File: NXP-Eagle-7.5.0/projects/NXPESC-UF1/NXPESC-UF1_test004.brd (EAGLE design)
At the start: 59.7 x 20.6 mm, 75 parts, among them P1 MOT_PWR_PAD-1, P2 MOT_PWR_PAD-1, P3 MOT_PWR_PAD-1, P4 MOT_PWR_PAD-1, P5 MOT_PWR_PAD-1, U1 DF13-4P-1.25H, U10 PSMN1R4-30YLD, U11 PSMN1R4-30YLD, U12 PSMN1R4-30YLD, U13 PSMN1R4-30YLD, U15 TJA1042TK/3, U17 DF13-4P-1.25H, U2 MKV31F512VLH12-M, U8 PSMN1R4-30YLD, U9 PSMN1R4-30YLD

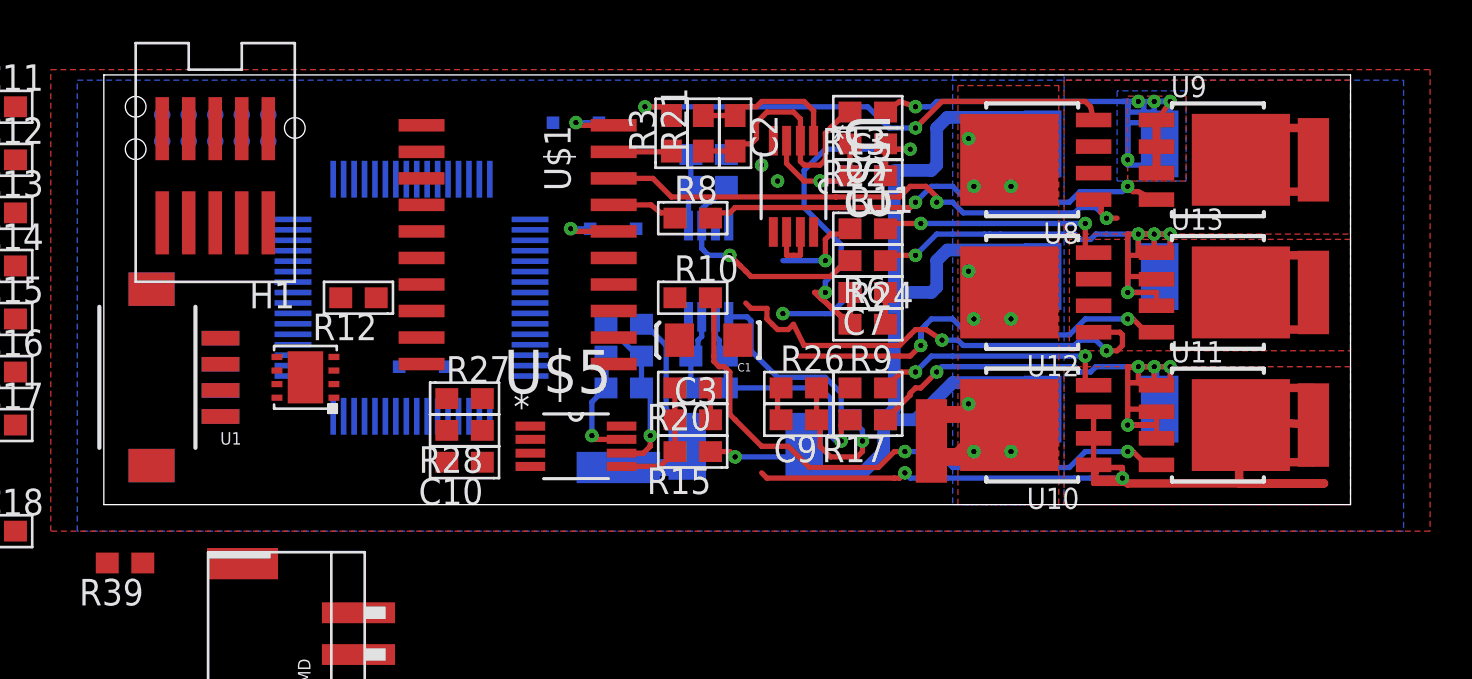
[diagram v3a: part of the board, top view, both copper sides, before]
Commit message: Majority of Power FET stage/gate driver and sense amplifiers are layed out. Moving on to finishing the MCU details.
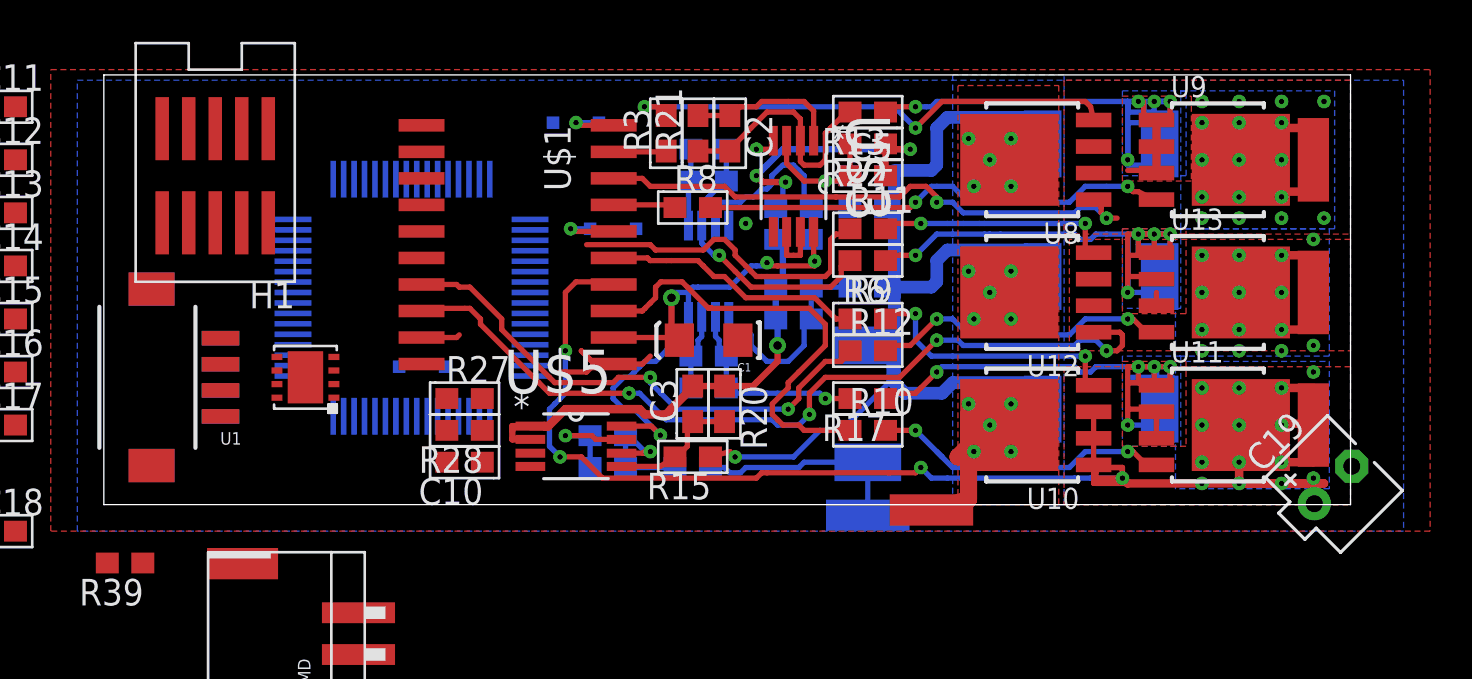
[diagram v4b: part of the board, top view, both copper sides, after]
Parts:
- removed H3: TC2050-IDCNH, etc-connector-003a:TC2050-IDC-NOHOLES
- added C19: (no value), etc-rcl:ETR1
- moved R12 24.5 mm to (36.6, 7.37), turned to 0 degrees
- moved P4 12.2 mm to (36.6, -0.51), turned to 180 degrees
- moved R10 10.5 mm to (36.6, 3.56)
- moved R16 7.61 mm to (28.2, 1.78)
- moved R18 6.35 mm to (36.6, 10.4)
- moved R5 6.19 mm to (36.6, 4.83), turned to 90 degrees
- moved C7 5.40 mm to (33.0, 14.2), flipped to the bottom, turned to 0 degrees
- moved R24 5.40 mm to (33.0, 12.7), flipped to the bottom, turned to 180 degrees
- moved C4 5.39 mm to (24.1, 1.78)
- moved C9 4.83 mm to (33.0, 8.89), flipped to the bottom, turned to 0 degrees
- moved R26 4.83 mm to (33.0, 10.4), flipped to the bottom, turned to 180 degrees
- moved R7 4.06 mm to (36.6, 14.2)
- moved R9 3.30 mm to (36.6, 8.89)
- moved P5 3.30 mm to (39.6, -0.25), turned to 0 degrees
- moved R19 2.41 mm to (24.1, 3.30)
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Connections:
- net +3V3: no longer H3.1
- net +V_MOTOR: now also C19.+
- net AGND: now also C19.-
- net GND: no longer H3.2, H3.3
- net RESET_B: no longer H3.6
- net SWD_CLK: no longer H3.9
- net SWD_DIO: no longer H3.10
- net TRACE_SWO: no longer H3.8
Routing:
- net +3V3: track 0.00 -> 27.4 mm, vias 0 -> 4
- net LOC: track 0.00 -> 25.1 mm, vias 0 -> 2
- net LOB: track 0.00 -> 21.9 mm
- net PH_B: track 61.5 -> 82.7 mm, vias 2 -> 18
- net PH_C: track 38.0 -> 56.4 mm, vias 2 -> 18
- net N$9: track 28.9 -> 14.6 mm
- net HOC: track 4.59 -> 17.7 mm, vias 1 -> 0
- net HOB: track 0.00 -> 12.5 mm
- net ADC_MID: track 30.6 -> 39.8 mm, vias 2 -> 4
- net GND: track 0.00 -> 7.87 mm
- net CS_C_L: track 5.28 -> 11.7 mm, vias 1 -> 0
- net N$17: track 20.7 -> 14.5 mm
- net CS_ABC_L/DCB_H: track 61.7 -> 56.0 mm
- net N$11: track 39.5 -> 45.0 mm
- net +V_MOTOR: track 8.55 -> 13.6 mm, vias 9 -> 15
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- added copper zone on layer 1, net N$11
- added copper zone on layer 16, net N$11
- added copper zone on layer 1, net N$12
- added copper zone on layer 16, net N$12
- added copper zone on layer 16, net PH_A
- added copper zone on layer 16, net PH_B
- added copper zone on layer 16, net PH_C

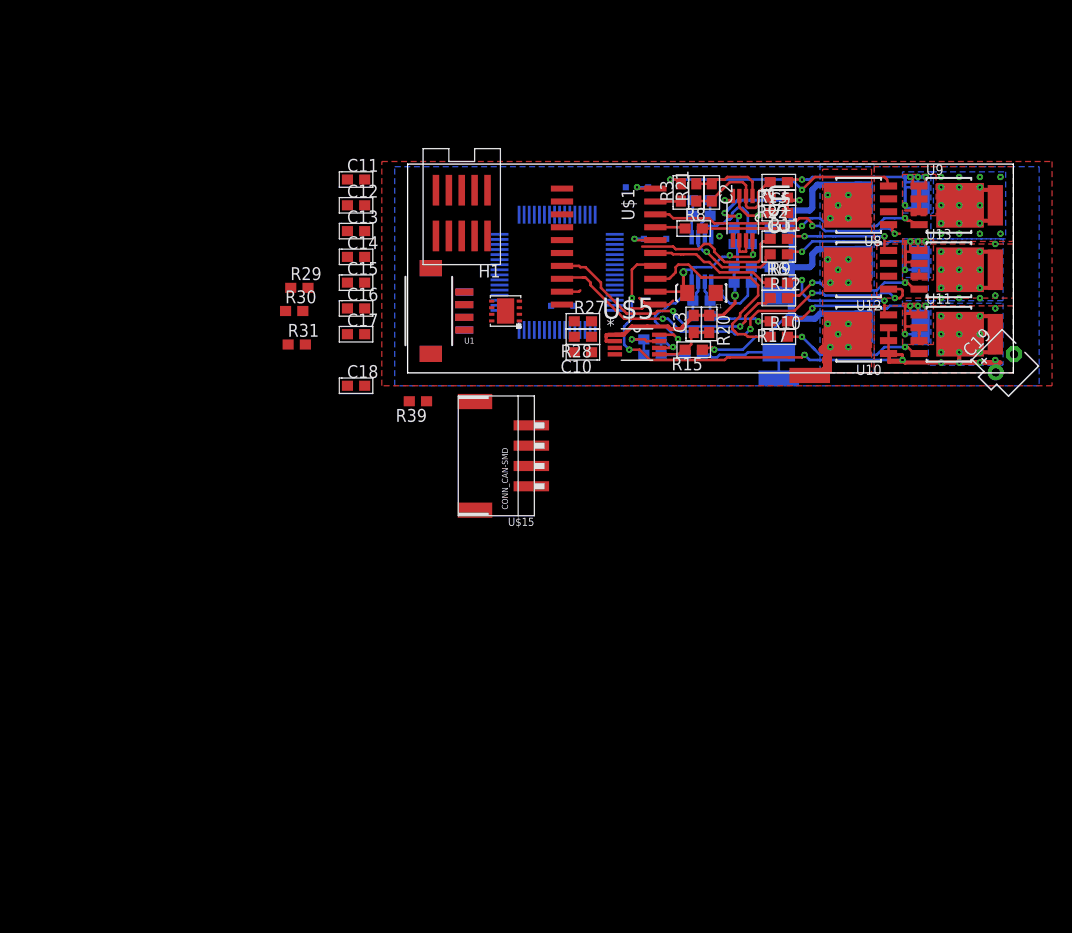
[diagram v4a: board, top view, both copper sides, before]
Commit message: Reviewing NXPESC-UF1/NXPESC-UF1_test004.sch schematic, comparing against SCHEMATICS-FRDM-mc-lvpmsm-sch.pdf
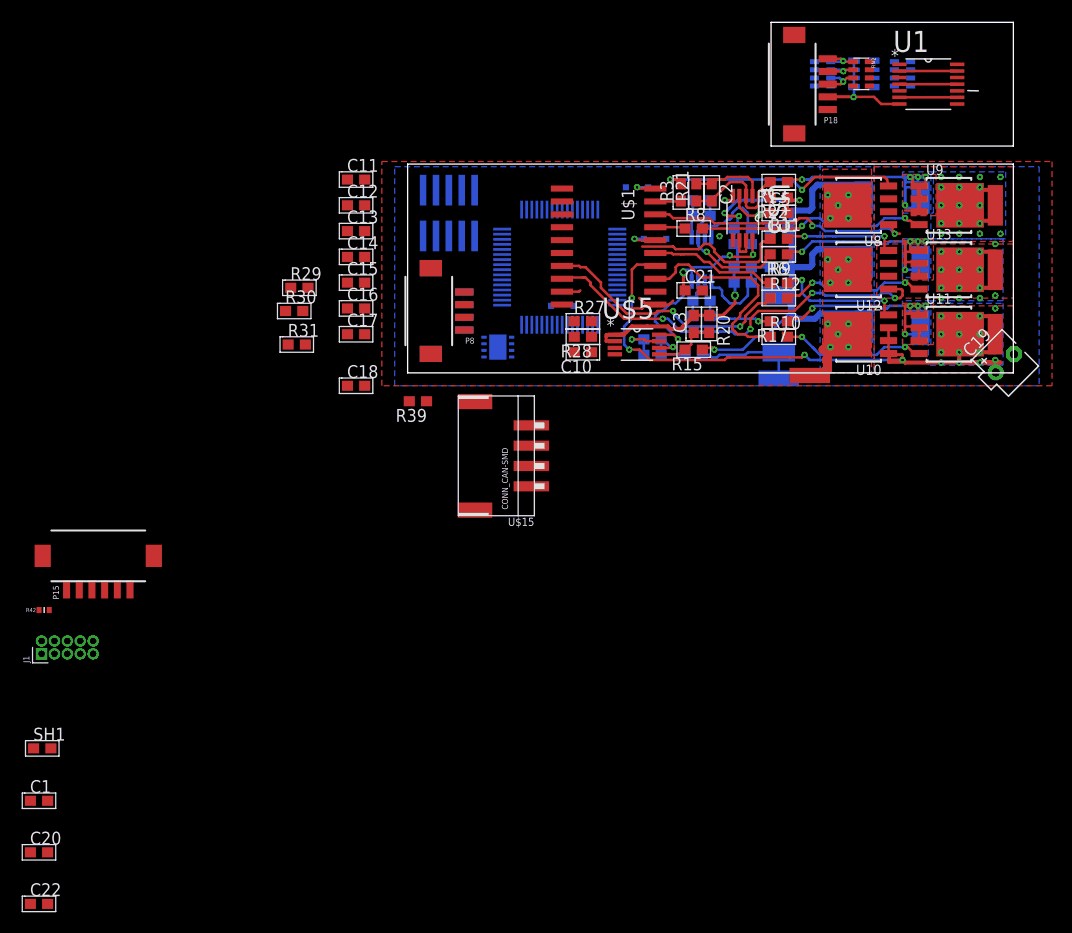
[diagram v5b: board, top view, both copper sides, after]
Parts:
- removed U17: DF13-4P-1.25H, pixhawk2:DF13A-4P-1.25H
- added C20, C21, C22: CAP0603-1UF-50V, etc-rcl:C0603
- added CA1: CCA-GNM-314R71C104MA01L, etc-rcl:RES_ARRAY_4I_S
- added J1: ARM_MINI_JTAG-TH, pixhawk2:FTSH-105-01-XXX-DV
- added P15: DF13-6P-1.25H, pixhawk2:DF13A-6P-1.25H
- added P18: DF13-5P-1.25H, pixhawk2:DF13A-5P-1.25H
- added P8, P9: DF13-4P-1.25H, pixhawk2:DF13A-4P-1.25H
- added R42: (no value), pixhawk2:0402-RES
- added RN1, RN2, RN3: CTS742C083, pixhawk2:CTS742C083
- added SH1: RESC0603-0R, etc-rcl:C0603
- C1: value Find a 50V -> CAP0603-1UF-50V; device pixhawk2:EIA3216 -> etc-rcl:C0603
- R29, R30, R31: value RESC0603-100R -> RESC0603-10R-1; device etc_rcl:C0603 -> etc-rcl:C0603
- U1: value DF13-4P-1.25H -> 74LVX14MTCX; device pixhawk2:DF13A-4P-1.25H -> 74LVX14MTCX:SOP65P640X120-14N
- moved C1 82.2 mm to (-36.3, -42.2), turned to 0 degrees
- moved U1 53.9 mm to (51.3, 28.4), turned to 0 degrees
- moved U15 3.64 mm to (8.89, 2.54), flipped to the bottom, turned to 270 degrees
- moved H1 1.27 mm to (4.06, 15.7), flipped to the bottom, turned to 0 degrees
- moved U2 0.57 mm to (15.0, 10.4)
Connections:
- removed net N$8: R29.1, R30.1, R31.1
- new net ENC_A: U1.8, U2.41
- new net ENC_B: U1.10, U2.42
- new net ENC_C: U1.12
- new net N$19: U1.13, U1.2
- new net N$20: CA1.PA1, RN2.8, RN3.4
- new net N$21: CA1.PB1, RN2.7, RN3.3
- new net N$22: CA1.PC1, RN2.6, RN3.2
- new net N$23: U1.11, U1.4
- new net N$24: U1.6, U1.9
- new net N$25: RN3.7, U1.1
- new net N$26: RN3.6, U1.3
- new net N$27: RN3.5, U1.5
- new net N$29: P18.3, RN1.3, RN2.3
- new net N$32: P18.4, RN1.2, RN2.2
- new net N$35: P18.5, RN1.1, RN2.1
- net +3V3: no longer C1.A, U$1.12
- net +5V: now also P18.1, P8.1, P9.1, RN1.6, RN1.7, RN1.8, U1.14; no longer U1.1, U17.1
- net +V_MOTOR: now also C21.1, R29.1, R30.1, R31.1, U$1.12
- net AGND: now also SH1.1
- net CANH: now also P8.2, P9.2; no longer U1.2, U17.2
- net CANL: now also P8.3, P9.3; no longer U1.3, U17.3
- net GND: now also C21.2, CA1.PA2, CA1.PB2, CA1.PC2, P18.2, P8.4, P9.4, SH1.2, U1.7; no longer C1.C, U1.4, U17.4
- net N$15: now also C1.1
- net N$16: now also C20.1
- net N$18: now also C22.1
- net PH_A: now also C1.2
- net PH_B: now also C20.2
- net PH_C: now also C22.2
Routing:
- net GND: track 7.87 -> 21.4 mm, vias 2 -> 3
- net N$24: track 0.00 -> 5.69 mm
- net N$23: track 0.00 -> 5.69 mm
- net N$19: track 0.00 -> 5.69 mm
- net N$29: track 0.00 -> 4.50 mm, vias 0 -> 1
- net N$35: track 0.00 -> 3.88 mm, vias 0 -> 1
- net N$32: track 0.00 -> 3.87 mm, vias 0 -> 1
- net +3V3: track 27.4 -> 24.2 mm
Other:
- board size 59.7 x 20.6 mm -> 59.7 x 34.5 mm

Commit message: Draft PDF viewable file for status update
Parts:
- moved J1 57.3 mm to (1.52, 15.5)
- moved C1 41.1 mm to (-28.4, -1.78)
- moved C20 41.1 mm to (-28.4, -6.86)
- moved SH1 41.1 mm to (-28.1, 3.39)
- moved C22 41.1 mm to (-28.4, -11.9)
- moved P15 41.1 mm to (-22.6, 22.4)
- moved R42 41.1 mm to (-27.9, 17.0)
- moved U$15 34.9 mm to (-17.3, 7.62)
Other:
- board text added: "Adjust board size for soldering wires and CAP"
- board text added: "Alternate connector types"
- board text added: "CAN Transceiver"
- board text added: "Electrolytic Capacitor"
- board text added: "KV11"
- board text added: "Optional Encoder input for Robotics"
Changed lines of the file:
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@@
 <?xml version="1.0" encoding="utf-8"?>
 <!DOCTYPE eagle SYSTEM "eagle.dtd">
-<eagle version="7.6.0">
+<eagle version="7.5.0">
 <drawing>
 <settings>
@@
 <layer number="27" name="tValues" color="7" fill="1" visible="no" active="yes"/>
 <layer number="28" name="bValues" color="7" fill="1" visible="no" active="yes"/>
-<layer number="29" name="tStop" color="7" fill="3" visible="no" active="yes"/>
+<layer number="29" name="tStop" color="7" fill="3" visible="yes" active="yes"/>
 <layer number="30" name="bStop" color="7" fill="6" visible="no" active="yes"/>
 <layer number="31" name="tCream" color="7" fill="4" visible="no" active="yes"/>
@@
 <layer number="46" name="Milling" color="3" fill="1" visible="no" active="yes"/>
 <layer number="47" name="Measures" color="7" fill="1" visible="no" active="yes"/>
-<layer number="48" name="Document" color="7" fill="1" visible="no" active="yes"/>
+<layer number="48" name="Document" color="7" fill="1" visible="yes" active="yes"/>
 <layer number="49" name="Reference" color="7" fill="1" visible="no" active="yes"/>
 <layer number="50" name="dxf" color="7" fill="1" visible="no" active="yes"/>
@@
 <wire x1="35.814" y1="34.544" x2="35.814" y2="22.352" width="0" layer="20"/>
 <rectangle x1="64" y1="0" x2="82" y2="22" layer="115"/>
+<text x="65.278" y="8.89" size="1.778" layer="48">Electrolytic
+Capacitor</text>
+<text x="64.77" y="-5.334" size="1.778" layer="48">Electrolytic
+Capacitor</text>
+<text x="9.652" y="27.94" size="1.778" layer="48">KV11</text>
+<text x="36.068" y="34.798" size="1.778" layer="48">Optional
+Encoder input
+for Robotics </text>
+<text x="-39.37" y="7.112" size="1.778" layer="48">Alternate
+connector
+types</text>
+<text x="35.56" y="-16.764" size="1.778" layer="48">Adjust board size
+for soldering
+wires and CAP</text>
+<wire x1="39.37" y1="-2.286" x2="39.37" y2="-3.81" width="0.4064" layer="48"/>
+<wire x1="39.37" y1="-3.81" x2="43.942" y2="-8.382" width="0.4064" layer="48"/>
+<wire x1="57.912" y1="-3.048" x2="57.912" y2="-4.318" width="0.4064" layer="48"/>
+<wire x1="57.912" y1="-4.318" x2="54.102" y2="-8.128" width="0.4064" layer="48"/>
+<text x="4.318" y="-8.89" size="1.778" layer="48">CAN
+Transceiver</text>
+<wire x1="5.588" y1="2.286" x2="5.588" y2="-2.54" width="0.4064" layer="48"/>
+<wire x1="5.588" y1="-2.54" x2="6.35" y2="-3.302" width="0.4064" layer="48"/>
 </plain>
 <attributes>
@@
 <element name="R31" library="etc-rcl" package="C0603" value="RESC0603-10R-1" x="-10.922" y="2.794"/>
 <element name="P8" library="pixhawk2" package="DF13A-4P-1.25H" value="DF13-4P-1.25H" x="2.286" y="6.096" rot="R90"/>
-<element name="U$15" library="pixhawk2" package="S4B-PH-SM4-TB" value="CONN_CAN-SMD" x="12.192" y="-11.176" rot="R90"/>
+<element name="U$15" library="pixhawk2" package="S4B-PH-SM4-TB" value="CONN_CAN-SMD" x="-17.272" y="7.62" rot="R90"/>
 <element name="P1" library="NXPHLITE" package="MPAD1" value="MOT_PWR_PAD-1" x="57.912" y="16.51" rot="R90"/>
 <element name="P2" library="NXPHLITE" package="MPAD1" value="MOT_PWR_PAD-1" x="57.912" y="3.81" rot="R90"/>
@@
 <element name="P5" library="NXPHLITE" package="MPAD1" value="MOT_PWR_PAD-1" x="39.624" y="-0.254"/>
 <element name="C19" library="etc-rcl" package="ETR1" value="" x="58.853603125" y="0.941603125" rot="R45"/>
-<element name="P15" library="pixhawk2" package="DF13A-6P-1.25H" value="DF13-6P-1.25H" x="-30.48" y="-18.034"/>
+<element name="P15" library="pixhawk2" package="DF13A-6P-1.25H" value="DF13-6P-1.25H" x="-22.606" y="22.352"/>
 <element name="U1" library="74LVX14MTCX" package="SOP65P640X120-14N" value="74LVX14MTCX" x="51.308" y="28.448"/>
 <element name="P18" library="pixhawk2" package="DF13A-5P-1.25H" value="DF13-5P-1.25H" x="38.1" y="28.448" rot="R90"/>
-<element name="R42" library="pixhawk2" package="0402-RES" value="" x="-35.814" y="-23.368"/>
-<element name="J1" library="pixhawk2" package="FTSH-105-01-XXX-DV" value="ARM_MINI_JTAG-TH" x="-36.068" y="-27.686"/>
+<element name="R42" library="pixhawk2" package="0402-RES" value="" x="-27.94" y="17.018"/>
+<element name="J1" library="pixhawk2" package="FTSH-105-01-XXX-DV" value="ARM_MINI_JTAG-TH" x="1.524" y="15.494"/>
 <element name="RN1" library="pixhawk2" package="CTS742C083" value="CTS742C083" x="40.894" y="29.464" rot="MR270">
 <attribute name="OC_NEWARK" value="unknown" x="40.894" y="29.464" size="1.778" layer="28" rot="MR270" display="off"/>
@@
 <attribute name="MF" value="" x="48.768" y="29.464" size="1.778" layer="28" rot="MR90" display="off"/>
 </element>
-<element name="SH1" library="etc-rcl" package="C0603" value="RESC0603-0R" x="-36" y="-37"/>
+<element name="SH1" library="etc-rcl" package="C0603" value="RESC0603-0R" x="-28.126" y="3.386"/>
 <element name="C21" library="etc-rcl" package="C0603" value="CAP0603-1UF-50V" x="28.194" y="8.128"/>
-<element name="C1" library="etc-rcl" package="C0603" value="CAP0603-1UF-50V" x="-36.322" y="-42.164"/>
-<element name="C20" library="etc-rcl" package="C0603" value="CAP0603-1UF-50V" x="-36.322" y="-47.244"/>
-<element name="C22" library="etc-rcl" package="C0603" value="CAP0603-1UF-50V" x="-36.322" y="-52.324"/>
+<element name="C1" library="etc-rcl" package="C0603" value="CAP0603-1UF-50V" x="-28.448" y="-1.778"/>
+<element name="C20" library="etc-rcl" package="C0603" value="CAP0603-1UF-50V" x="-28.448" y="-6.858"/>
+<element name="C22" library="etc-rcl" package="C0603" value="CAP0603-1UF-50V" x="-28.448" y="-11.938"/>
 </elements>
 <signals>
@@
 <contactref element="SH1" pad="2"/>
 <contactref element="C21" pad="2"/>
-<wire x1="-4.23" y1="-1.27" x2="-35.15" y2="-37" width="0" layer="19" extent="1-1"/>
+<wire x1="-4.23" y1="-1.27" x2="-27.276" y2="3.386" width="0" layer="19" extent="1-1"/>
 <wire x1="-4.23" y1="3.81" x2="-4.23" y2="-1.27" width="0" layer="19" extent="1-1"/>
 <wire x1="-4.23" y1="6.35" x2="-4.23" y2="3.81" width="0" layer="19" extent="1-1"/>
@@
 <via x="54.356" y="14.732" extent="1-16" drill="0.254"/>
 <contactref element="C1" pad="2"/>
-<wire x1="24.412" y1="15.621" x2="-35.472" y2="-42.164" width="0" layer="19" extent="1-1"/>
+<wire x1="24.412" y1="15.621" x2="-27.598" y2="-1.778" width="0" layer="19" extent="1-1"/>
 </signal>
 <signal name="PH_B">
@@
 <via x="52.578" y="1.016" extent="1-16" drill="0.254"/>
 <contactref element="C20" pad="2"/>
-<wire x1="21.336" y1="2.794" x2="-35.472" y2="-47.244" width="0" layer="19" extent="1-16"/>
+<wire x1="21.336" y1="2.794" x2="-27.598" y2="-6.858" width="0" layer="19" extent="1-16"/>
 </signal>
 <signal name="PH_C">
@@
 <via x="56.388" y="7.366" extent="1-16" drill="0.254"/>
 <contactref element="C22" pad="2"/>
-<wire x1="15.212" y1="9.271" x2="-35.472" y2="-52.324" width="0" layer="19" extent="1-1"/>
+<wire x1="15.212" y1="9.271" x2="-27.598" y2="-11.938" width="0" layer="19" extent="1-1"/>
 </signal>
 <signal name="N$1">
@@
 <wire x1="29.718" y1="1.778" x2="29.044" y2="1.778" width="0.254" layer="16"/>
 <contactref element="SH1" pad="1"/>
-<wire x1="29.044" y1="1.778" x2="-36.85" y2="-37" width="0" layer="19" extent="1-16"/>
+<wire x1="29.044" y1="1.778" x2="-28.976" y2="3.386" width="0" layer="19" extent="1-16"/>
 <wire x1="59.751628125" y1="1.839628125" x2="36.576" y2="2.026" width="0" layer="19" extent="16-16"/>
 </signal>
@@
 <wire x1="22.606" y1="18.288" x2="23.706" y2="18.288" width="0.254" layer="16"/>
 <contactref element="C1" pad="1"/>
-<wire x1="22.733" y1="18.161" x2="-37.172" y2="-42.164" width="0" layer="19" extent="1-1"/>
+<wire x1="22.733" y1="18.161" x2="-29.298" y2="-1.778" width="0" layer="19" extent="1-1"/>
 </signal>
 <signal name="N$16">
@@
 <wire x1="22.352" y1="13.208" x2="23.284" y2="13.208" width="0.254" layer="16"/>
 <contactref element="C20" pad="1"/>
-<wire x1="22.479" y1="13.081" x2="-37.172" y2="-47.244" width="0" layer="19" extent="1-1"/>
+<wire x1="22.479" y1="13.081" x2="-29.298" y2="-6.858" width="0" layer="19" extent="1-1"/>
 </signal>
 <signal name="N$18">
@@
 <contactref element="D1" pad="C"/>
 <contactref element="C22" pad="1"/>
-<wire x1="14.14" y1="6.604" x2="-37.172" y2="-52.324" width="0" layer="19" extent="1-16"/>
+<wire x1="14.14" y1="6.604" x2="-29.298" y2="-11.938" width="0" layer="19" extent="1-16"/>
 <wire x1="15.212" y1="6.731" x2="14.14" y2="6.604" width="0" layer="19" extent="1-16"/>
 </signal>
@@
 </board>
 </drawing>
+<compatibility>
+<note version="6.3" minversion="6.2.2" severity="warning">
+Since Version 6.2.2 text objects can contain more than one line,
+which will not be processed correctly with this version.
+</note>
+</compatibility>
 </eagle>
